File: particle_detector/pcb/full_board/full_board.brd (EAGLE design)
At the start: 64 x 32 mm, 42 parts, among them IC1 LT1807R, IC2 TLV3501, IC3 LT3461, IC4 TEENSY 3.2, IC5 SENSL-SIPM

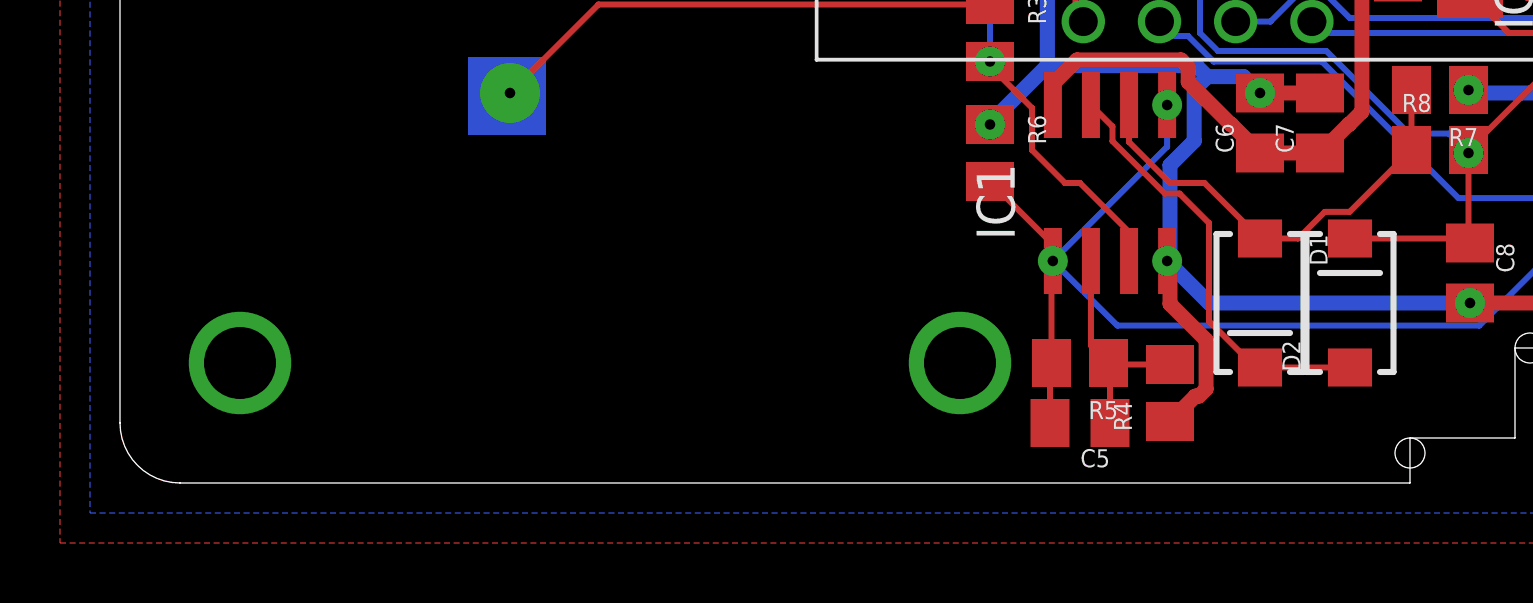
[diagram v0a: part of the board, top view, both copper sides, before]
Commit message: fix traces; this board needs to be flipped to conform to the ICD
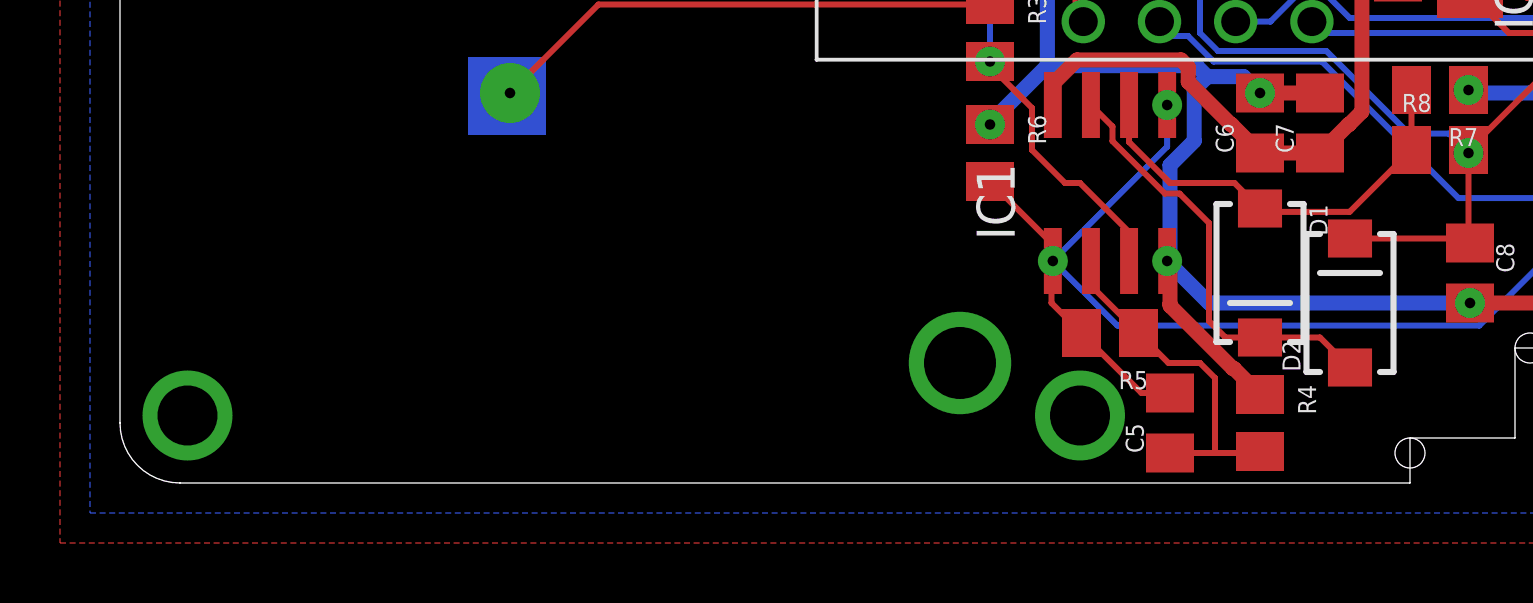
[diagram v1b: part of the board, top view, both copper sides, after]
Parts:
- moved R4 3.16 mm to (38.0, 2.00), turned to 270 degrees
- moved C5 3.00 mm to (35.0, 2.00), turned to 90 degrees
- moved R5 1.41 mm to (33.0, 5.00)
- moved D1 1.00 mm to (38.0, 7.00)
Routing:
- net N$8: track 7.66 -> 11.7 mm
- net SIG_AMP: track 59.8 -> 61.0 mm
- net N$4: track 15.2 -> 14.5 mm
- net AGND: track 78.5 -> 77.8 mm

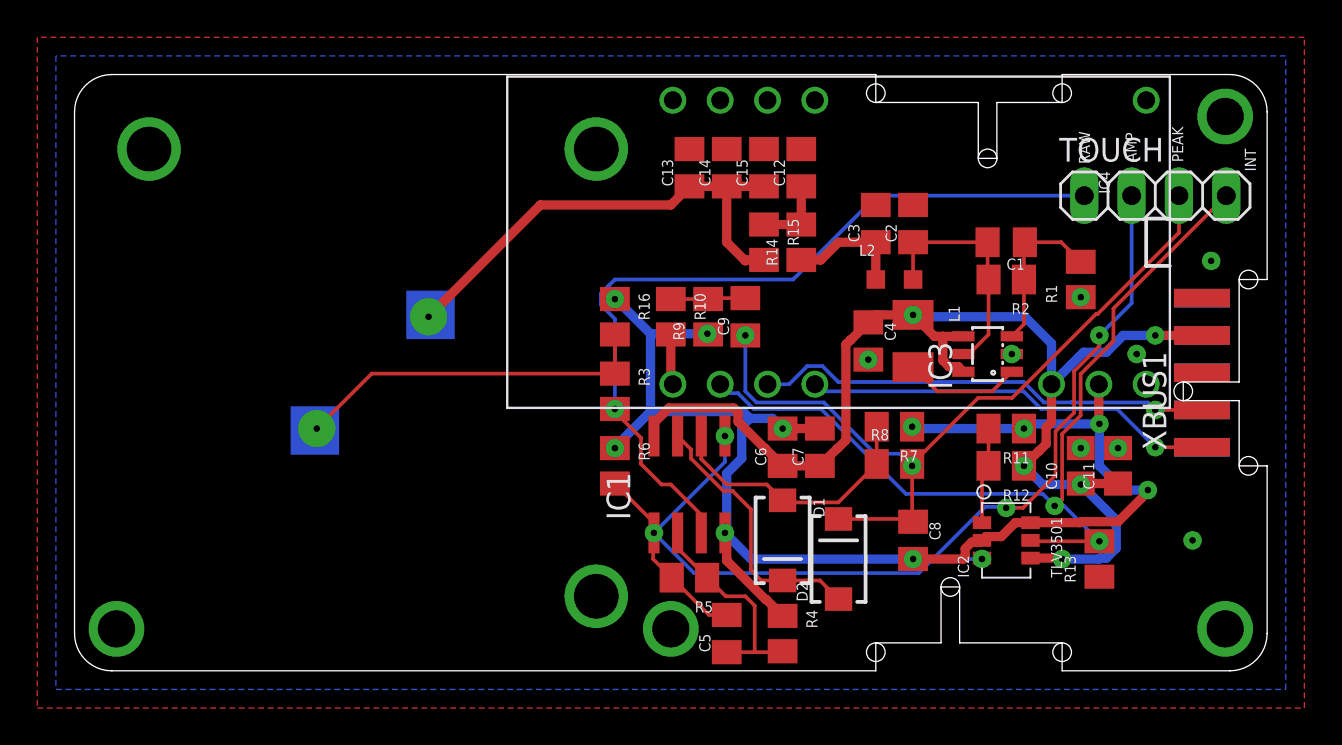
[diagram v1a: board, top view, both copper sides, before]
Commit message: finish full board; still needs Serial connnections (sent to PCBWay 2019.05.19)
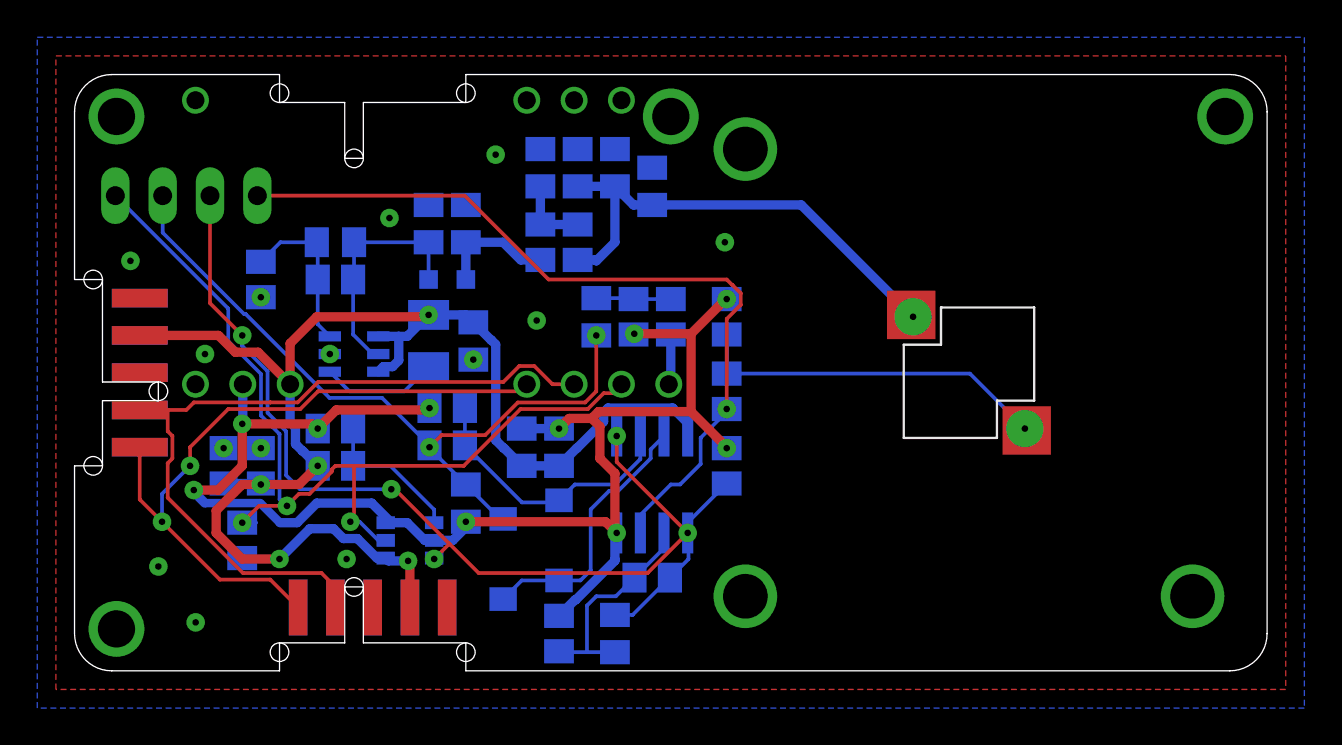
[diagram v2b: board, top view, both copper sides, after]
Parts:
- added XBUS2: (no value), personal:XBUS_2X05_PAD
- IC4: device personal:TEENSY_3.1_FOR_THINSAT -> personal:TEENSY_3.2_THINSAT
- XBUS1: device personal:XBUS_1X05_PAD -> personal:XBUS_2X05_PAD
- moved XBUS1 57.0 mm to (3.50, 16.0)
- moved TOUCH 52.0 mm to (6.00, 25.5), flipped to the bottom
- moved C11 48.0 mm to (8.00, 11.0), flipped to the bottom
- moved R13 46.0 mm to (9.00, 7.00), flipped to the bottom
- moved C10 44.0 mm to (10.0, 11.0), flipped to the bottom
- moved R1 44.0 mm to (10.0, 21.0), flipped to the bottom
- moved C1 36.0 mm to (14.0, 23.0), flipped to the bottom
- moved R11 36.0 mm to (14.0, 13.0), flipped to the bottom
- moved R12 36.0 mm to (14.0, 11.0), flipped to the bottom
- moved R2 36.0 mm to (14.0, 21.0), flipped to the bottom
- moved IC3 34.0 mm to (15.0, 17.0), flipped to the bottom
- moved IC2 32.0 mm to (18.0, 7.00), flipped to the bottom
- moved IC5 32.0 mm to (48.0, 16.0), flipped to the top
- moved C2 26.0 mm to (19.0, 24.0), flipped to the bottom
- moved L1 26.0 mm to (19.0, 17.7), flipped to the bottom
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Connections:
- net 3.3V: now also XBUS1.4, XBUS2.4; no longer XBUS1.P4B, XBUS1.P4T
- net GND: now also XBUS1.3, XBUS2.3; no longer XBUS1.P3B, XBUS1.P3T
- net SCL: now also XBUS1.1, XBUS2.1; no longer XBUS1.P1B, XBUS1.P1T
- net SDA: now also XBUS1.2, XBUS2.2; no longer XBUS1.P2B, XBUS1.P2T
- net VBAT: now also XBUS1.5, XBUS2.5; no longer XBUS1.P5B, XBUS1.P5T
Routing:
- net SDA: track 24.7 -> 41.7 mm, vias 1 -> 0
- net SCL: track 22.2 -> 37.8 mm, vias 1 -> 2
- net 3.3V: track 67.8 -> 77.7 mm
- net N$5: track 5.19 -> 8.02 mm
- net SIG_PEAK: track 42.3 -> 40.0 mm
- net SIG_INT: track 48.7 -> 50.8 mm, vias 2 -> 3
- net SIG_AMP: track 61.0 -> 59.5 mm
- net AGND: track 77.8 -> 78.9 mm
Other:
- outline, holes or cut-outs redrawn
